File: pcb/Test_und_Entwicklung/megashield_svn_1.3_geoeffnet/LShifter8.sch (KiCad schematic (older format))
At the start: 3 parts, among them Q30 BBS138

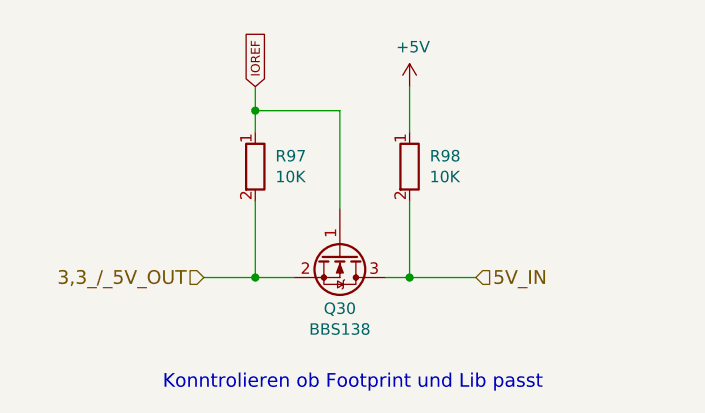
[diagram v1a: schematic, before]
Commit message: megashield_svn_1.3_geoeffnet
megashield_svn_1.3_geoeffnet
Diverse Änderungen
Schutzschaltung teilweise entfernt
300 Ohm Widerstand eingefügt
9V Pinleite hinzugefügt - wir über das Laderelais geschaltet
Leiterbahnen teileweise neu verlegt
Beidseitiges GND Flächengitter hinzugefügt
Levelschifter Ultraschall Trigger hinzugefügt
usw.....
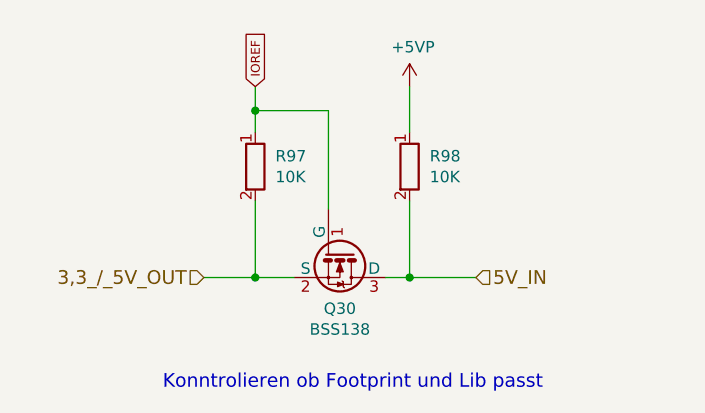
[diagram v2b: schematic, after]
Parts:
- removed Q30: BBS138, TO_SOT_Packages_SMD:SOT-23, symbol Q_NMOS_GSD
- added Q30: BSS138, TO_SOT_Packages_SMD:SOT-23, symbol BSS138
- R97, R98: footprint Resistors_SMD:R_0805 -> Zimprich:R_0603
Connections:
- net 3,3_/_5V_OUT: now also Q30.2 (S)
- net 5V_IN: now also Q30.3 (D)
- net IOREF: now also Q30.1 (G)
- net +5V renamed +5VP
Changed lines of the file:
@@
 $Descr A4 11693 8268
 encoding utf-8
-Sheet 19 28
+Sheet 19 31
 Title ""
-Date ""
+Date "2017-02-17"
 Rev ""
 Comp ""
@@
 F 0 "R98" H 6198 3296 50  0000 L CNN
 F 1 "10K" H 6198 3205 50  0000 L CNN
-F 2 "Resistors_SMD:R_0805" V 6040 3250 50  0001 C CNN
+F 2 "Zimprich:R_0603" V 6040 3250 50  0001 C CNN
 F 3 "Value" H 6110 3250 50  0001 C CNN
 F 4 "Value" H 6198 3371 60  0001 L CNN "Gehäuseart"
@@
 F 0 "R97" H 5523 3296 50  0000 L CNN
 F 1 "10K" H 5523 3205 50  0000 L CNN
-F 2 "Resistors_SMD:R_0805" V 5365 3250 50  0001 C CNN
+F 2 "Zimprich:R_0603" V 5365 3250 50  0001 C CNN
 F 3 "Value" H 5435 3250 50  0001 C CNN
 F 4 "Value" H 5523 3371 60  0001 L CNN "Gehäuseart"
@@
 Wire Wire Line
 	6110 3100 6110 2900
-$Comp
-L +5V #PWR?
-U 1 1 57E6FFF9
-P 6110 2900
-AR Path="/57DC7E7B/57E6FB3B/57E6FFF9" Ref="#PWR?"  Part="1"
-AR Path="/57DC7E7B/57E78D37/57E6FFF9" Ref="#PWR?"  Part="1"
-AR Path="/57DC7E7B/57E712F4/57E6FFF9" Ref="#PWR?"  Part="1"
-AR Path="/57DC7E7B/57E71CBC/57E6FFF9" Ref="#PWR?"  Part="1"
-AR Path="/57DC7E7B/582A0806/57E6FFF9" Ref="#PWR0140"  Part="1"
-F 0 "#PWR0140" H 6110 2750 50  0001 C CNN
-F 1 "+5V" H 6125 3073 50  0000 C CNN
-F 2 "" H 6110 2900 50  0000 C CNN
-F 3 "" H 6110 2900 50  0000 C CNN
-	1    6110 2900
-	1    0    0    -1
-$EndComp
 Wire Wire Line
 	5435 3100 5435 2900
-Wire Wire Line
-	5805 3435 5805 3005
-Wire Wire Line
-	5805 3005 5435 3005
-Connection ~ 5435 3005
 $Bitmap
 Pos -6080 2610
@@
 EndData
 $EndBitmap
-$Comp
-L Q_NMOS_GSD Q?
-U 1 1 57E6FFFB
-P 5805 3635
-AR Path="/57DC7E7B/57E6FB3B/57E6FFFB" Ref="Q?"  Part="1"
-AR Path="/57DC7E7B/57E78D37/57E6FFFB" Ref="Q?"  Part="1"
-AR Path="/57DC7E7B/57E712F4/57E6FFFB" Ref="Q?"  Part="1"
-AR Path="/57DC7E7B/57E71CBC/57E6FFFB" Ref="Q?"  Part="1"
-AR Path="/57DC7E7B/582A0806/57E6FFFB" Ref="Q30"  Part="1"
-F 0 "Q30" V 6041 3635 50  0000 C CNN
-F 1 "BBS138" V 6132 3635 50  0000 C CNN
-F 2 "TO_SOT_Packages_SMD:SOT-23" V 6223 3635 50  0001 C CNN
-F 3 "Value" H 5805 3635 50  0001 C CNN
-F 4 "Value" V 6322 3635 60  0001 C CNN "Gehäuseart"
-F 5 "Value" V 6428 3635 60  0001 C CNN "Bestelllink"
-F 6 "Value" V 6534 3635 60  0001 C CNN "Technische Daten"
-F 7 "Value" V 6640 3635 60  0001 C CNN "Bestellnummer"
-F 8 "Value" V 6746 3635 60  0001 C CNN "Bauform"
-	1    5805 3635
-	0    1    1    0
-$EndComp
 Text Notes 5030 4230 0    60   ~ 0
 Konntrolieren ob Footprint und Lib passt
 Text GLabel 5435 2900 1    39   Input ~ 0
 IOREF
+$Comp
+L BSS138 Q30
+U 1 1 58AB0AE8
+P 5805 3635
+F 0 "Q30" V 6041 3635 50  0000 C CNN
+F 1 "BSS138" V 6132 3635 50  0000 C CNN
+F 2 "TO_SOT_Packages_SMD:SOT-23" H -810 335 50  0001 L CIN
+F 3 "" H -1010 410 50  0001 L CNN
+	1    5805 3635
+	0    1    1    0
+$EndComp
+Wire Wire Line
+	5755 3435 5755 3005
+Wire Wire Line
+	5755 3005 5435 3005
+Connection ~ 5435 3005
+$Comp
+L +5VP #PWR0141
+U 1 1 58AB0E19
+P 6110 2900
+F 0 "#PWR0141" H -420 -85 50  0001 C CNN
+F 1 "+5VP" H 6125 3073 50  0000 C CNN
+F 2 "" H -420 65  50  0001 C CNN
+F 3 "" H -420 65  50  0001 C CNN
+	1    6110 2900
+	1    0    0    -1
+$EndComp
 $EndSCHEMATC

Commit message: megashield_svn_1.3_geoeffnet
Alternativer Platz für Summer hinzu gefügt. - Unterhalb des Mega auf der
Rückseite der Platine.
Der Hauptsummer sitzt evl auf der Rückseite hinter dem Bumperduino
ungünstig weil er abgedeckt wird
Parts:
- Q30: symbol BSS138 -> BSS138-RESCUE-ardumower_mega_shield_svn
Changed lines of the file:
@@
 IOREF
 $Comp
-L BSS138 Q30
+L BSS138-RESCUE-ardumower_mega_shield_svn Q30
 U 1 1 58AB0AE8
 P 5805 3635
@@
 Connection ~ 5435 3005
 $Comp
-L +5VP #PWR0156
+L +5VP #PWR0157
 U 1 1 58AB0E19
 P 6110 2900
-F 0 "#PWR0156" H -420 -85 50  0001 C CNN
+F 0 "#PWR0157" H -420 -85 50  0001 C CNN
 F 1 "+5VP" H 6125 3073 50  0000 C CNN
 F 2 "" H -420 65  50  0001 C CNN
